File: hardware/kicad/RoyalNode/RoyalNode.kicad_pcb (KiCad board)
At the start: 4 copper layers, 85 x 75 mm, 71 parts, among them J1 XT30PW-M C431092 RC, J2 XT30PW-M C431092 RC, J3 J_LOW_JST_GH_SM02B_GHS_TB_RC, J4 J_LOW_JST_GH_SM02B_GHS_TB_RC, J5 SMA edge envelope, J6 J_LOW_JST_GH_SM04B_GHS_TB_RC, Q1 Infineon PG-DSO-8-27 thermal 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, Q2 Infineon PG-DSO-8-27 thermal 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, Q3 Infineon PG-DSO-8-27 thermal 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, U1 BQ25798 RQM0029A RC, U2 LM66100 DCK0006A SC70-6 RC, U3 TPS61088 RHL0020A thermal via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, U4 LTC4365 TSOT-23-8 RC

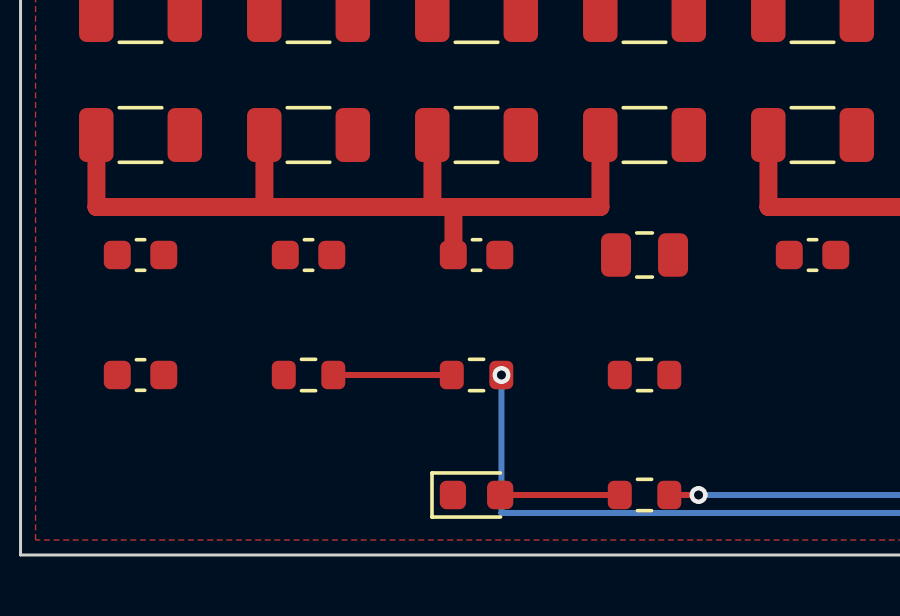
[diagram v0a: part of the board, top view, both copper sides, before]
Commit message: Route BQ REGN local passive link
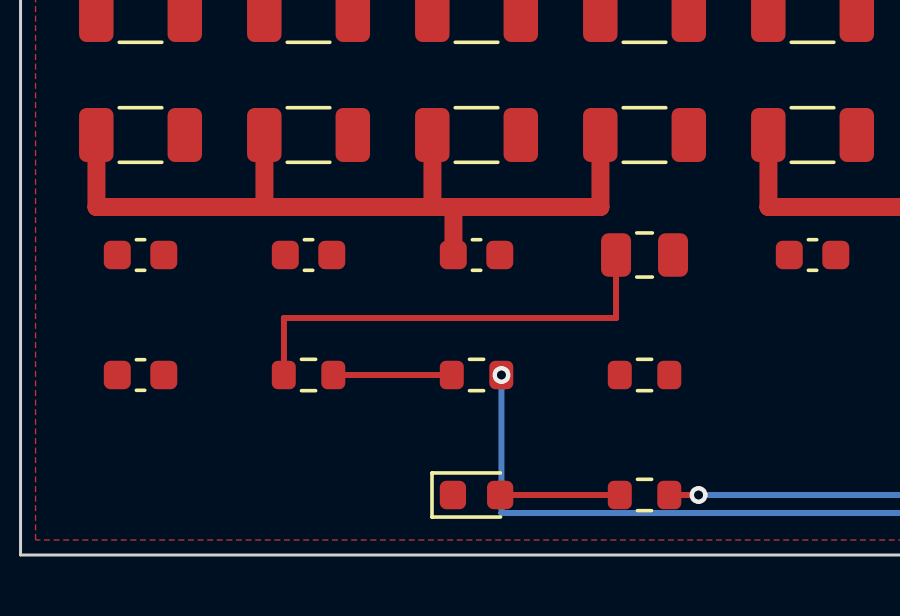
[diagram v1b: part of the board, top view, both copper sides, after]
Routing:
- net BQ_REGN: track 0.00 -> 15.1 mm
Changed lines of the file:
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@@
+	)
+	(segment
+		(start 28.78 87.1)
+		(end 39.85 87.1)
+		(width 0.2)
+		(layer "F.Cu")
+		(net "BQ_REGN")
+	)
+	(segment
+		(start 39.85 87.1)
+		(end 39.85 85)
+		(width 0.2)
+		(layer "F.Cu")
+		(net "BQ_REGN")
+	)
+	(segment
+		(start 28.78 89)
+		(end 28.78 87.1)
+		(width 0.2)
+		(layer "F.Cu")
+		(net "BQ_REGN")
 	)
 	(segment

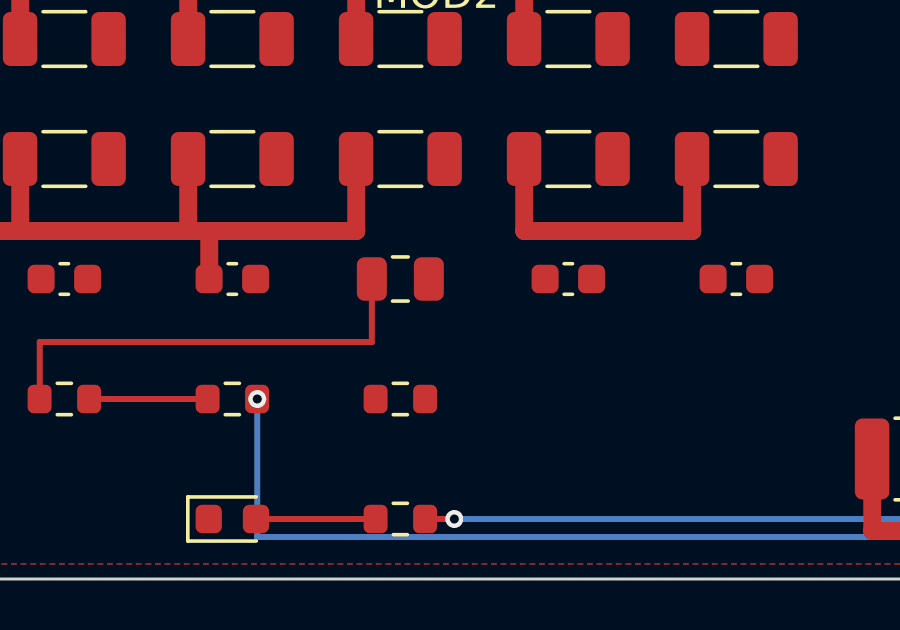
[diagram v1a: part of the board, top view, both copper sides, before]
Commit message: Route BAT RAW sense branch
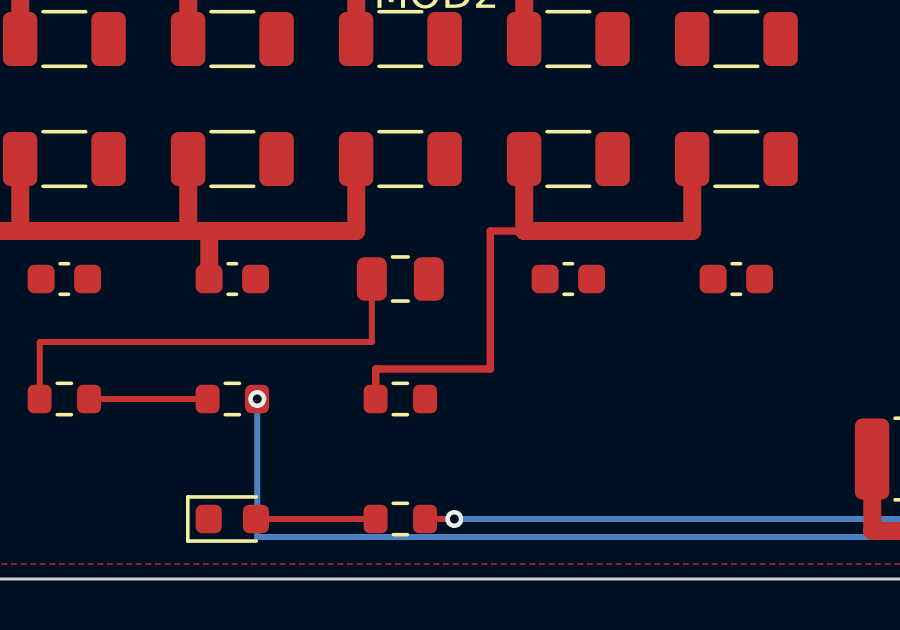
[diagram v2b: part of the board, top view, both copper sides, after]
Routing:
- net BAT_RAW: track 10.8 -> 21.4 mm
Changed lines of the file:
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@@
+	)
+	(segment
+		(start 43.8 83.4)
+		(end 44.93 83.4)
+		(width 0.25)
+		(layer "F.Cu")
+		(net "BAT_RAW")
 	)
 	(segment
@@
 	)
 	(segment
+		(start 39.98 88)
+		(end 43.8 88)
+		(width 0.25)
+		(layer "F.Cu")
+		(net "BAT_RAW")
+	)
+	(segment
+		(start 39.98 89)
+		(end 39.98 88)
+		(width 0.25)
+		(layer "F.Cu")
+		(net "BAT_RAW")
+	)
+	(segment
 		(start 44.93 81)
 		(end 44.93 83.4)
@@
 		(layer "F.Cu")
 		(net "BAT_RAW")
+	)
+	(segment
+		(start 43.8 88)
+		(end 43.8 83.4)
+		(width 0.25)
+		(layer "F.Cu")
+		(net "BAT_RAW")

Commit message: Route BQ VBUS C212 jog
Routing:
- net BQ_VBUS: track 23.7 -> 37.8 mm, vias 2 -> 4
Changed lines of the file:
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@@
+	(segment
+		(start 22.53 75)
+		(end 21.4 75)
+		(width 0.2)
+		(layer "F.Cu")
+		(net "BQ_VBUS")
+	)
 	(segment
 		(start 22.53 75)
@@
 	)
 	(segment
+		(start 22.4 85.8)
+		(end 23.23 85)
+		(width 0.2)
+		(layer "F.Cu")
+		(net "BQ_VBUS")
+	)
+	(segment
 		(start 22.53 77)
 		(end 22.53 75)
 		(width 0.6)
 		(layer "F.Cu")
+		(net "BQ_VBUS")
+	)
+	(via
+		(at 22.4 85.8)
+		(size 0.6)
+		(drill 0.3)
+		(layers "F.Cu" "B.Cu")
+		(net "BQ_VBUS")
+	)
+	(via
+		(at 21.4 75)
+		(size 0.6)
+		(drill 0.3)
+		(layers "F.Cu" "B.Cu")
 		(net "BQ_VBUS")
 	)
@@
 		(net "BQ_VBUS")
 	)
+	(segment
+		(start 21.4 75)
+		(end 21.4 85.8)
+		(width 0.2)
+		(layer "B.Cu")
+		(net "BQ_VBUS")
+	)
+	(segment
+		(start 21.4 85.8)
+		(end 22.4 85.8)
+		(width 0.2)
+		(layer "B.Cu")
+		(net "BQ_VBUS")
+	)

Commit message: Route BQ PMID C213 jog
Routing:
- net BQ_PMID: track 17.2 -> 35.6 mm, vias 0 -> 2
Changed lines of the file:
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@@
+	(segment
+		(start 33.73 75)
+		(end 32.6 75)
+		(width 0.2)
+		(layer "F.Cu")
+		(net "BQ_PMID")
+	)
 	(segment
 		(start 33.73 75)
@@
 		(net "BQ_PMID")
 	)
+	(segment
+		(start 27.6 85.8)
+		(end 28.83 85)
+		(width 0.2)
+		(layer "F.Cu")
+		(net "BQ_PMID")
+	)
+	(via
+		(at 27.6 85.8)
+		(size 0.6)
+		(drill 0.3)
+		(layers "F.Cu" "B.Cu")
+		(net "BQ_PMID")
+	)
+	(via
+		(at 32.6 75)
+		(size 0.6)
+		(drill 0.3)
+		(layers "F.Cu" "B.Cu")
+		(net "BQ_PMID")
+	)
+	(segment
+		(start 27.6 75)
+		(end 27.6 85.8)
+		(width 0.2)
+		(layer "B.Cu")
+		(net "BQ_PMID")
+	)
+	(segment
+		(start 32.6 75)
+		(end 27.6 75)
+		(width 0.2)
+		(layer "B.Cu")
+		(net "BQ_PMID")
+	)

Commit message: Route boost 5V feedback sense link
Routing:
- net 5V_RADIO: track 51.4 -> 56.6 mm
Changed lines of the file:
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@@
+	)
+	(segment
+		(start 39.83 26.6)
+		(end 40.48 26.6)
+		(width 0.2)
+		(layer "F.Cu")
+		(net "5V_RADIO")
 	)
 	(segment
@@
 	)
 	(segment
+		(start 39.83 24.5)
+		(end 39.83 26.6)
+		(width 0.2)
+		(layer "F.Cu")
+		(net "5V_RADIO")
+	)
+	(segment
 		(start 57.35 54.25)
 		(end 57.35 55.25)
@@
 		(layer "F.Cu")
 		(net "5V_RADIO")
+	)
+	(segment
+		(start 40.48 26.6)
+		(end 40.48 29)
+		(width 0.2)
+		(layer "F.Cu")
+		(net "5V_RADIO")

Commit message: Route solar fused divider link
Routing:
- net SOLAR_FUSED: track 15.1 -> 27.1 mm, vias 2 -> 4
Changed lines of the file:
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@@
+	)
+	(segment
+		(start 25.98 43.7)
+		(end 25.98 42.8)
+		(width 0.2)
+		(layer "F.Cu")
+		(net "SOLAR_FUSED")
 	)
 	(segment
@@
 		(end 80.63 54.1)
 		(width 0.8)
+		(layer "F.Cu")
+		(net "SOLAR_FUSED")
+	)
+	(segment
+		(start 21.18 38)
+		(end 21.18 39)
+		(width 0.2)
 		(layer "F.Cu")
 		(net "SOLAR_FUSED")
@@
 	)
 	(via
+		(at 25.98 43.7)
+		(size 0.6)
+		(drill 0.3)
+		(layers "F.Cu" "B.Cu")
+		(net "SOLAR_FUSED")
+	)
+	(via
 		(at 89.6 54)
 		(size 0.6)
 		(drill 0.3)
 		(layers "F.Cu" "B.Cu")
+		(net "SOLAR_FUSED")
+	)
+	(via
+		(at 21.18 39)
+		(size 0.6)
+		(drill 0.3)
+		(layers "F.Cu" "B.Cu")
+		(net "SOLAR_FUSED")
+	)
+	(segment
+		(start 25.98 44)
+		(end 25.98 43.7)
+		(width 0.2)
+		(layer "B.Cu")
 		(net "SOLAR_FUSED")
 	)
@@
 		(layer "B.Cu")
 		(net "SOLAR_FUSED")
+	)
+	(segment
+		(start 21.18 39)
+		(end 21.18 44)
+		(width 0.2)
+		(layer "B.Cu")
+		(net "SOLAR_FUSED")
+	)
+	(segment
+		(start 21.18 44)
+		(end 25.98 44)
+		(width 0.2)
+		(layer "B.Cu")
+		(net "SOLAR_FUSED")

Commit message: Route BQ SYS C205 jog
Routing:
- net BQ_SYS: track 37.6 -> 54.8 mm, vias 0 -> 2
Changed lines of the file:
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@@
+	)
+	(segment
+		(start 50 77.8)
+		(end 50.53 77)
+		(width 0.3)
+		(layer "F.Cu")
+		(net "BQ_SYS")
 	)
 	(segment
@@
 		(net "BQ_SYS")
 	)
+	(segment
+		(start 39.33 83.4)
+		(end 40.5 83.4)
+		(width 0.3)
+		(layer "F.Cu")
+		(net "BQ_SYS")
+	)
+	(via
+		(at 40.5 83.4)
+		(size 0.6)
+		(drill 0.3)
+		(layers "F.Cu" "B.Cu")
+		(net "BQ_SYS")
+	)
+	(via
+		(at 50 77.8)
+		(size 0.6)
+		(drill 0.3)
+		(layers "F.Cu" "B.Cu")
+		(net "BQ_SYS")
+	)
+	(segment
+		(start 40.5 79)
+		(end 50 79)
+		(width 0.3)
+		(layer "B.Cu")
+		(net "BQ_SYS")
+	)
+	(segment
+		(start 50 79)
+		(end 50 77.8)
+		(width 0.3)
+		(layer "B.Cu")
+		(net "BQ_SYS")
+	)
+	(segment
+		(start 40.5 83.4)
+		(end 40.5 79)
+		(width 0.3)
+		(layer "B.Cu")
+		(net "BQ_SYS")
+	)

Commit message: Route BQ SYS C404 bridge
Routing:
- net BQ_SYS: track 54.8 -> 76.3 mm, vias 2 -> 4
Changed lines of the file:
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@@
+	)
+	(segment
+		(start 46.13 22.5)
+		(end 46.13 24.5)
+		(width 0.3)
+		(layer "F.Cu")
+		(net "BQ_SYS")
 	)
 	(segment
@@
 		(net "BQ_SYS")
 	)
+	(via
+		(at 46.13 22.5)
+		(size 0.6)
+		(drill 0.3)
+		(layers "F.Cu" "B.Cu")
+		(net "BQ_SYS")
+	)
+	(via
+		(at 28.63 22.5)
+		(size 0.6)
+		(drill 0.3)
+		(layers "F.Cu" "B.Cu")
+		(net "BQ_SYS")
+	)
+	(segment
+		(start 28.63 22.5)
+		(end 28.63 21.5)
+		(width 0.3)
+		(layer "B.Cu")
+		(net "BQ_SYS")
+	)
 	(segment
 		(start 40.5 79)
@@
 	)
 	(segment
+		(start 46.13 21.5)
+		(end 46.13 22.5)
+		(width 0.3)
+		(layer "B.Cu")
+		(net "BQ_SYS")
+	)
+	(segment
 		(start 40.5 83.4)
 		(end 40.5 79)
 		(width 0.3)
 		(layer "B.Cu")
+		(net "BQ_SYS")
+	)
+	(segment
+		(start 28.63 21.5)
+		(end 46.13 21.5)
+		(width 0.3)
+		(layer "B.Cu")
